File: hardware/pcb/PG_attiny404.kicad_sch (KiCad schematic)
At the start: 30 parts, among them J1 0022232041, J2 Conn_01x01_Male, J3 Conn_01x01_Male, J4 Conn_01x01_Male, J5 Conn_01x01_Male, J6 Conn_01x01_Male, J7 Conn_01x01_Male, J8 Conn_01x01_Male, J9 Conn_01x01_Male, Q1 2N7002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

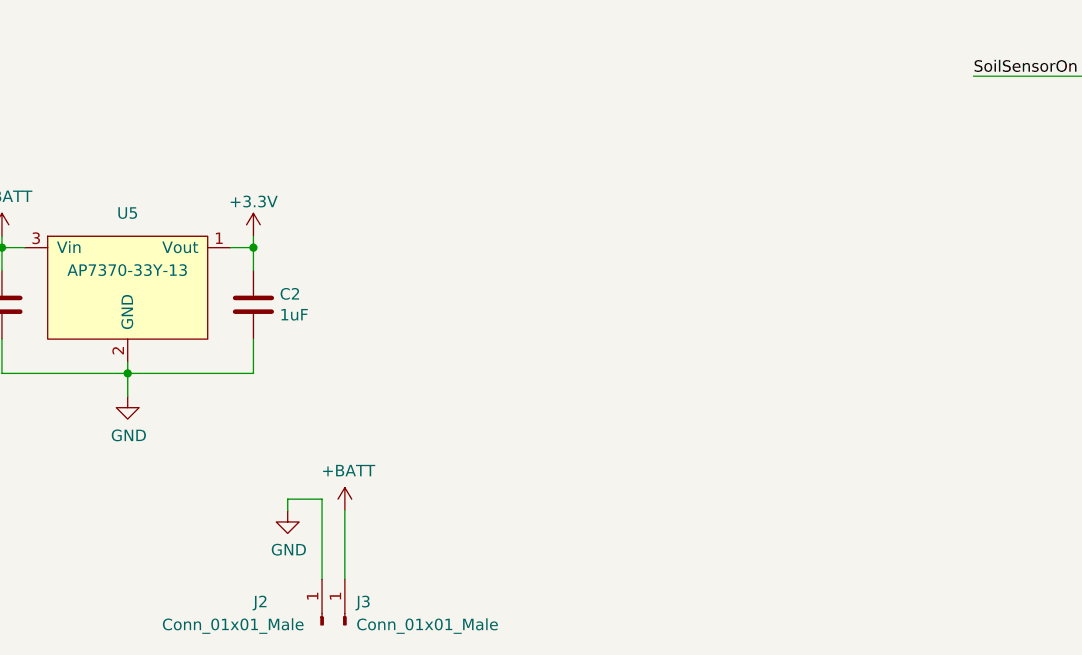
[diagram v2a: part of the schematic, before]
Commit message: Added Reverse voltage protection on PCB
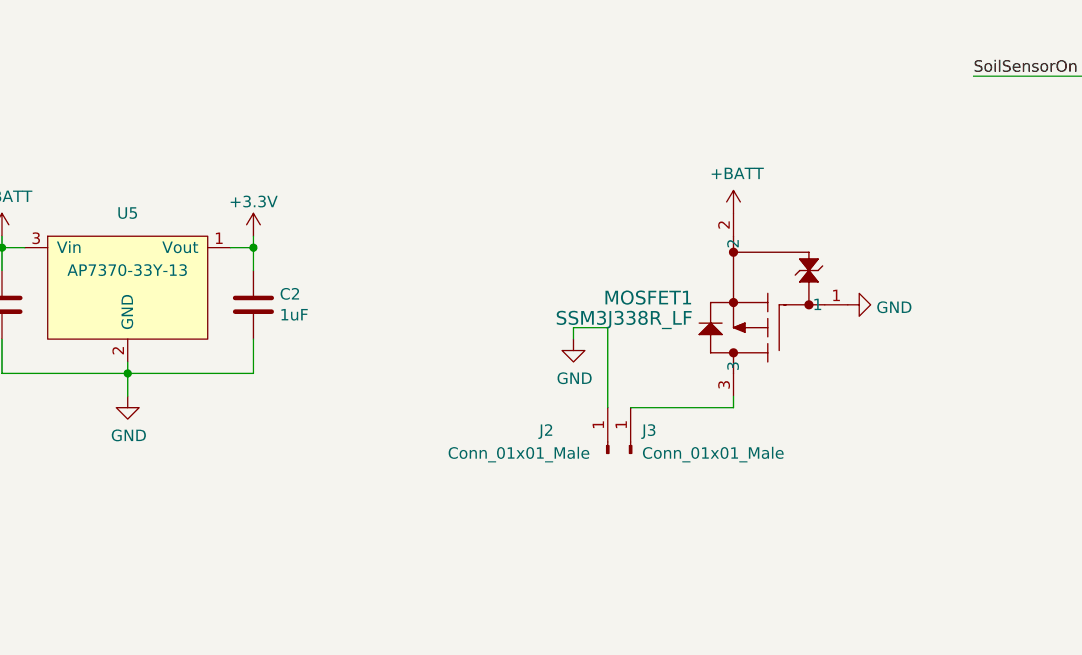
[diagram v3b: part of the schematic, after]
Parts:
- added MOSFET1: SSM3J338R_LF, SOT23:SOT-23F_TOS-L, symbol SSM3J338R_LF:SSM3J338R_LF
- J1: footprint Connector_PinHeader_2.54mm:PinHeader_1x04_P2.54mm_Horizontal -> SOT23:PinHeader_1x04_P2.54mm_Horizontal_spezial
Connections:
- net +BATT: now also MOSFET1.2; no longer J3.1 (Pin_1)
- net GND: now also MOSFET1.1
- new net: J3.1 (Pin_1), MOSFET1.3
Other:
- moved on the sheet: J2, J3
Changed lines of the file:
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@@
+    (stroke (width 0) (type default))
+  )
+  (wire (pts (xy 96.52 168.91) (xy 107.95 168.91))
     (stroke (width 0) (type default))
   )
@@
     (stroke (width 0) (type default))
   )
+  (wire (pts (xy 107.95 168.91) (xy 107.95 167.64))
+    (stroke (width 0) (type default))
+  )
   (wire (pts (xy 132.08 113.03) (xy 156.21 113.03))
     (stroke (width 0) (type default))
@@
     (stroke (width 0) (type default))
   )
-  (wire (pts (xy 62.23 179.07) (xy 62.23 187.96))
+  (wire (pts (xy 93.98 160.02) (xy 93.98 168.91))
     (stroke (width 0) (type default))
   )
@@
     (stroke (width 0) (type default))
   )
-  (wire (pts (xy 58.42 179.07) (xy 58.42 180.34))
+  (wire (pts (xy 90.17 160.02) (xy 90.17 161.29))
     (stroke (width 0) (type default))
   )
@@
     (stroke (width 0) (type default))
   )
-  (wire (pts (xy 62.23 179.07) (xy 58.42 179.07))
+  (wire (pts (xy 93.98 160.02) (xy 90.17 160.02))
     (stroke (width 0) (type default))
   )
@@
   )
   (wire (pts (xy 26.67 161.29) (xy 26.67 165.1))
-    (stroke (width 0) (type default))
-  )
-  (wire (pts (xy 64.77 180.34) (xy 64.77 187.96))
     (stroke (width 0) (type default))
   )
@@
       (effects (font (size 1.27 1.27)) (justify right))
     )
-    (property "Footprint" "Connector_PinHeader_2.54mm:PinHeader_1x04_P2.54mm_Horizontal" (at 109.22 49.53 0)
+    (property "Footprint" "SOT23:PinHeader_1x04_P2.54mm_Horizontal_spezial" (at 109.22 49.53 0)
       (effects (font (size 1.524 1.524)) (justify left) hide)
     )
@@
     )
   )
-  (symbol (lib_id "Connector:Conn_01x01_Male") (at 62.23 193.04 90) (unit 1)
-    (in_bom yes) (on_board yes) (dnp no)
-    (property "Reference" "J2" (at 54.61 190.5 90)
-      (effects (font (size 1.27 1.27)) (justify right))
-    )
-    (property "Value" "Conn_01x01_Male" (at 44.45 193.04 90)
-      (effects (font (size 1.27 1.27)) (justify right))
-    )
-    (property "Footprint" "digikey-footprints:PROBE_PAD_1206" (at 62.23 193.04 0)
-      (effects (font (size 1.27 1.27)) hide)
-    )
-    (property "Datasheet" "~" (at 62.23 193.04 0)
+  (symbol (lib_id "Connector:Conn_01x01_Male") (at 93.98 173.99 90) (unit 1)
+    (in_bom yes) (on_board yes) (dnp no)
+    (property "Reference" "J2" (at 86.36 171.45 90)
+      (effects (font (size 1.27 1.27)) (justify right))
+    )
+    (property "Value" "Conn_01x01_Male" (at 76.2 173.99 90)
+      (effects (font (size 1.27 1.27)) (justify right))
+    )
+    (property "Footprint" "digikey-footprints:PROBE_PAD_1206" (at 93.98 173.99 0)
+      (effects (font (size 1.27 1.27)) hide)
+    )
+    (property "Datasheet" "~" (at 93.98 173.99 0)
       (effects (font (size 1.27 1.27)) hide)
     )
@@
     )
   )
-  (symbol (lib_id "Connector:Conn_01x01_Male") (at 64.77 193.04 90) (unit 1)
-    (in_bom yes) (on_board yes) (dnp no)
-    (property "Reference" "J3" (at 66.04 190.5 90)
-      (effects (font (size 1.27 1.27)) (justify right))
-    )
-    (property "Value" "Conn_01x01_Male" (at 66.04 193.04 90)
-      (effects (font (size 1.27 1.27)) (justify right))
-    )
-    (property "Footprint" "digikey-footprints:PROBE_PAD_1206" (at 64.77 193.04 0)
-      (effects (font (size 1.27 1.27)) hide)
-    )
-    (property "Datasheet" "~" (at 64.77 193.04 0)
+  (symbol (lib_id "Connector:Conn_01x01_Male") (at 96.52 173.99 90) (unit 1)
+    (in_bom yes) (on_board yes) (dnp no)
+    (property "Reference" "J3" (at 97.79 171.45 90)
+      (effects (font (size 1.27 1.27)) (justify right))
+    )
+    (property "Value" "Conn_01x01_Male" (at 97.79 173.99 90)
+      (effects (font (size 1.27 1.27)) (justify right))
+    )
+    (property "Footprint" "digikey-footprints:PROBE_PAD_1206" (at 96.52 173.99 0)
+      (effects (font (size 1.27 1.27)) hide)
+    )
+    (property "Datasheet" "~" (at 96.52 173.99 0)
       (effects (font (size 1.27 1.27)) hide)
     )
@@
     )
   )
-  (symbol (lib_id "power:+BATT") (at 64.77 180.34 0) (unit 1)
-    (in_bom yes) (on_board yes) (dnp no)
-    (property "Reference" "#PWR016" (at 64.77 184.15 0)
-      (effects (font (size 1.27 1.27)) hide)
-    )
-    (property "Value" "+BATT" (at 65.151 175.9458 0)
-      (effects (font (size 1.27 1.27)))
-    )
-    (property "Footprint" "" (at 64.77 180.34 0)
-      (effects (font (size 1.27 1.27)) hide)
-    )
-    (property "Datasheet" "" (at 64.77 180.34 0)
+  (symbol (lib_id "power:+BATT") (at 107.95 147.32 0) (unit 1)
+    (in_bom yes) (on_board yes) (dnp no)
+    (property "Reference" "#PWR016" (at 107.95 151.13 0)
+      (effects (font (size 1.27 1.27)) hide)
+    )
+    (property "Value" "+BATT" (at 108.331 142.9258 0)
+      (effects (font (size 1.27 1.27)))
+    )
+    (property "Footprint" "" (at 107.95 147.32 0)
+      (effects (font (size 1.27 1.27)) hide)
+    )
+    (property "Datasheet" "" (at 107.95 147.32 0)
       (effects (font (size 1.27 1.27)) hide)
     )
@@
     )
   )
-  (symbol (lib_id "power:GND") (at 58.42 180.34 0) (unit 1)
-    (in_bom yes) (on_board yes) (dnp no)
-    (property "Reference" "#PWR015" (at 58.42 186.69 0)
-      (effects (font (size 1.27 1.27)) hide)
-    )
-    (property "Value" "GND" (at 58.547 184.7342 0)
-      (effects (font (size 1.27 1.27)))
-    )
-    (property "Footprint" "" (at 58.42 180.34 0)
-      (effects (font (size 1.27 1.27)) hide)
-    )
-    (property "Datasheet" "" (at 58.42 180.34 0)
+  (symbol (lib_id "power:GND") (at 90.17 161.29 0) (unit 1)
+    (in_bom yes) (on_board yes) (dnp no)
+    (property "Reference" "#PWR015" (at 90.17 167.64 0)
+      (effects (font (size 1.27 1.27)) hide)
+    )
+    (property "Value" "GND" (at 90.297 165.6842 0)
+      (effects (font (size 1.27 1.27)))
+    )
+    (property "Footprint" "" (at 90.17 161.29 0)
+      (effects (font (size 1.27 1.27)) hide)
+    )
+    (property "Datasheet" "" (at 90.17 161.29 0)
       (effects (font (size 1.27 1.27)) hide)
     )
@@
         (path "/e68a78e5-8846-4666-9105-5fa8784d19c8"
           (reference "D1") (unit 1)
+        )
+      )
+    )
+  )
+  (symbol (lib_name "GND_1") (lib_id "power:GND") (at 120.65 157.48 90) (unit 1)
+    (in_bom yes) (on_board yes) (dnp no) (fields_autoplaced)
+    (property "Reference" "#PWR020" (at 127 157.48 0)
+      (effects (font (size 1.27 1.27)) hide)
+    )
+    (property "Value" "GND" (at 123.825 157.7968 90)
+      (effects (font (size 1.27 1.27)) (justify right))
+    )
+    (property "Footprint" "" (at 120.65 157.48 0)
+      (effects (font (size 1.27 1.27)) hide)
+    )
+    (property "Datasheet" "" (at 120.65 157.48 0)
+      (effects (font (size 1.27 1.27)) hide)
+    )
+    (pin "1")
+    (instances
+      (project "PG_attiny404"
+        (path "/e68a78e5-8846-4666-9105-5fa8784d19c8"
+          (reference "#PWR020") (unit 1)
         )
       )
@@
         )
       )
+    )
+  )
+  (symbol (lib_id "SSM3J338R_LF:SSM3J338R_LF") (at 118.11 165.1 180) (unit 1)
+    (in_bom yes) (on_board yes) (dnp no) (fields_autoplaced)
+    (property "Reference" "MOSFET1" (at 103.4289 156.733 0)
+      (effects (font (size 1.524 1.524)) (justify left))
+    )
+    (property "Value" "SSM3J338R_LF" (at 103.4289 158.9872 0)
+      (effects (font (size 1.524 1.524)) (justify left))
+    )
+    (property "Footprint" "SOT23:SOT-23F_TOS-L" (at 118.11 165.1 0)
+      (effects (font (size 1.27 1.27) italic) hide)
+    )
+    (property "Datasheet" "SSM3J338R_LF" (at 118.11 165.1 0)
+      (effects (font (size 1.27 1.27) italic) hide)
+    )
+    (property "DK_Detail_Page" "https://www.digikey.at/de/products/detail/toshiba-semiconductor-and-storage/SSM3J338R-LF/5810226" (at 118.11 165.1 0)
+      (effects (font (size 1.27 1.27)) hide)
+    )
+    (pin "1")
+    (pin "2")
+    (pin "3")
+    (instances
+      (project "PG_attiny404"
+        (path "/e68a78e5-8846-4666-9105-5fa8784d19c8"
+          (reference "MOSFET1") (unit 1)
+        )
+      )

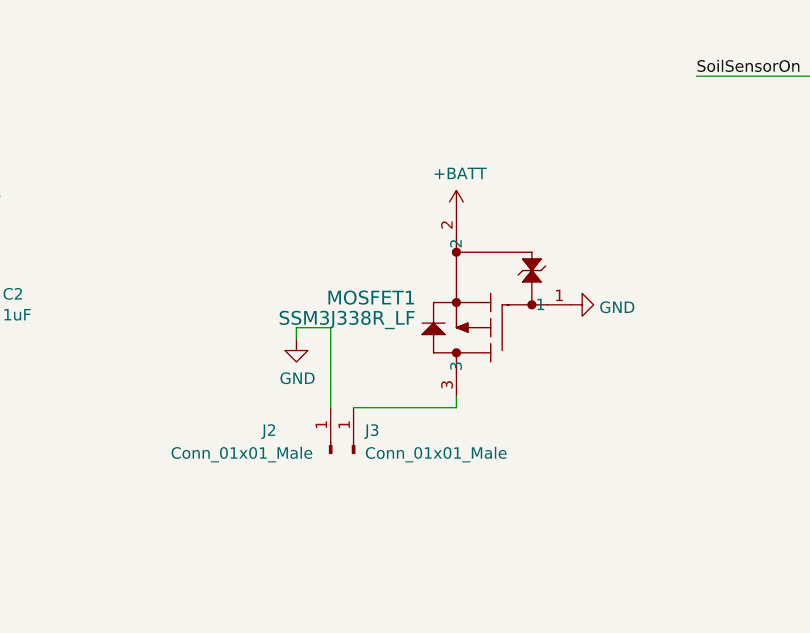
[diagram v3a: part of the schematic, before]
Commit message: Motor code polishing, Added p-channel to pcb for reverse voltage protection
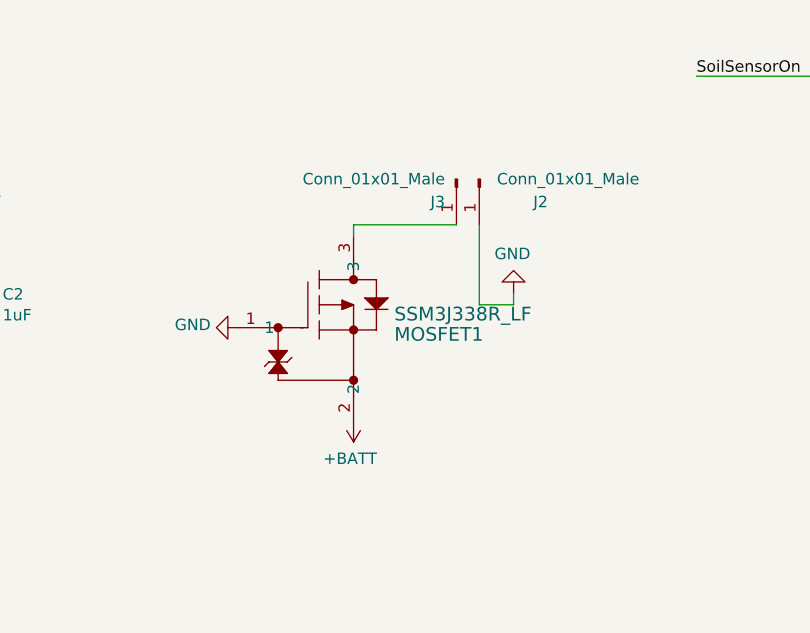
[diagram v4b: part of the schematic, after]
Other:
- moved on the sheet: J2, J3, MOSFET1
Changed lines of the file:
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@@
     (stroke (width 0) (type default))
   )
-  (wire (pts (xy 96.52 168.91) (xy 107.95 168.91))
+  (wire (pts (xy 107.95 148.59) (xy 96.52 148.59))
     (stroke (width 0) (type default))
   )
@@
     (stroke (width 0) (type default))
   )
-  (wire (pts (xy 107.95 168.91) (xy 107.95 167.64))
+  (wire (pts (xy 96.52 148.59) (xy 96.52 149.86))
     (stroke (width 0) (type default))
   )
@@
     (stroke (width 0) (type default))
   )
-  (wire (pts (xy 93.98 160.02) (xy 93.98 168.91))
+  (wire (pts (xy 110.49 157.48) (xy 110.49 148.59))
     (stroke (width 0) (type default))
   )
@@
     (stroke (width 0) (type default))
   )
-  (wire (pts (xy 90.17 160.02) (xy 90.17 161.29))
+  (wire (pts (xy 114.3 157.48) (xy 114.3 156.21))
     (stroke (width 0) (type default))
   )
@@
     (stroke (width 0) (type default))
   )
-  (wire (pts (xy 93.98 160.02) (xy 90.17 160.02))
+  (wire (pts (xy 110.49 157.48) (xy 114.3 157.48))
     (stroke (width 0) (type default))
   )
@@
     )
   )
-  (symbol (lib_id "Connector:Conn_01x01_Male") (at 93.98 173.99 90) (unit 1)
-    (in_bom yes) (on_board yes) (dnp no)
-    (property "Reference" "J2" (at 86.36 171.45 90)
-      (effects (font (size 1.27 1.27)) (justify right))
-    )
-    (property "Value" "Conn_01x01_Male" (at 76.2 173.99 90)
-      (effects (font (size 1.27 1.27)) (justify right))
-    )
-    (property "Footprint" "digikey-footprints:PROBE_PAD_1206" (at 93.98 173.99 0)
-      (effects (font (size 1.27 1.27)) hide)
-    )
-    (property "Datasheet" "~" (at 93.98 173.99 0)
+  (symbol (lib_id "Connector:Conn_01x01_Male") (at 110.49 143.51 270) (unit 1)
+    (in_bom yes) (on_board yes) (dnp no)
+    (property "Reference" "J2" (at 118.11 146.05 90)
+      (effects (font (size 1.27 1.27)) (justify right))
+    )
+    (property "Value" "Conn_01x01_Male" (at 128.27 143.51 90)
+      (effects (font (size 1.27 1.27)) (justify right))
+    )
+    (property "Footprint" "digikey-footprints:PROBE_PAD_1206" (at 110.49 143.51 0)
+      (effects (font (size 1.27 1.27)) hide)
+    )
+    (property "Datasheet" "~" (at 110.49 143.51 0)
       (effects (font (size 1.27 1.27)) hide)
     )
@@
     )
   )
-  (symbol (lib_id "Connector:Conn_01x01_Male") (at 96.52 173.99 90) (unit 1)
-    (in_bom yes) (on_board yes) (dnp no)
-    (property "Reference" "J3" (at 97.79 171.45 90)
-      (effects (font (size 1.27 1.27)) (justify right))
-    )
-    (property "Value" "Conn_01x01_Male" (at 97.79 173.99 90)
-      (effects (font (size 1.27 1.27)) (justify right))
-    )
-    (property "Footprint" "digikey-footprints:PROBE_PAD_1206" (at 96.52 173.99 0)
-      (effects (font (size 1.27 1.27)) hide)
-    )
-    (property "Datasheet" "~" (at 96.52 173.99 0)
+  (symbol (lib_id "Connector:Conn_01x01_Male") (at 107.95 143.51 270) (unit 1)
+    (in_bom yes) (on_board yes) (dnp no)
+    (property "Reference" "J3" (at 106.68 146.05 90)
+      (effects (font (size 1.27 1.27)) (justify right))
+    )
+    (property "Value" "Conn_01x01_Male" (at 106.68 143.51 90)
+      (effects (font (size 1.27 1.27)) (justify right))
+    )
+    (property "Footprint" "digikey-footprints:PROBE_PAD_1206" (at 107.95 143.51 0)
+      (effects (font (size 1.27 1.27)) hide)
+    )
+    (property "Datasheet" "~" (at 107.95 143.51 0)
       (effects (font (size 1.27 1.27)) hide)
     )
@@
     )
   )
-  (symbol (lib_id "power:+BATT") (at 107.95 147.32 0) (unit 1)
-    (in_bom yes) (on_board yes) (dnp no)
-    (property "Reference" "#PWR016" (at 107.95 151.13 0)
-      (effects (font (size 1.27 1.27)) hide)
-    )
-    (property "Value" "+BATT" (at 108.331 142.9258 0)
-      (effects (font (size 1.27 1.27)))
-    )
-    (property "Footprint" "" (at 107.95 147.32 0)
-      (effects (font (size 1.27 1.27)) hide)
-    )
-    (property "Datasheet" "" (at 107.95 147.32 0)
+  (symbol (lib_id "power:+BATT") (at 96.52 170.18 180) (unit 1)
+    (in_bom yes) (on_board yes) (dnp no)
+    (property "Reference" "#PWR016" (at 96.52 166.37 0)
+      (effects (font (size 1.27 1.27)) hide)
+    )
+    (property "Value" "+BATT" (at 96.139 174.5742 0)
+      (effects (font (size 1.27 1.27)))
+    )
+    (property "Footprint" "" (at 96.52 170.18 0)
+      (effects (font (size 1.27 1.27)) hide)
+    )
+    (property "Datasheet" "" (at 96.52 170.18 0)
       (effects (font (size 1.27 1.27)) hide)
     )
@@
     )
   )
-  (symbol (lib_id "power:GND") (at 90.17 161.29 0) (unit 1)
-    (in_bom yes) (on_board yes) (dnp no)
-    (property "Reference" "#PWR015" (at 90.17 167.64 0)
-      (effects (font (size 1.27 1.27)) hide)
-    )
-    (property "Value" "GND" (at 90.297 165.6842 0)
-      (effects (font (size 1.27 1.27)))
-    )
-    (property "Footprint" "" (at 90.17 161.29 0)
-      (effects (font (size 1.27 1.27)) hide)
-    )
-    (property "Datasheet" "" (at 90.17 161.29 0)
+  (symbol (lib_id "power:GND") (at 114.3 156.21 180) (unit 1)
+    (in_bom yes) (on_board yes) (dnp no)
+    (property "Reference" "#PWR015" (at 114.3 149.86 0)
+      (effects (font (size 1.27 1.27)) hide)
+    )
+    (property "Value" "GND" (at 114.173 151.8158 0)
+      (effects (font (size 1.27 1.27)))
+    )
+    (property "Footprint" "" (at 114.3 156.21 0)
+      (effects (font (size 1.27 1.27)) hide)
+    )
+    (property "Datasheet" "" (at 114.3 156.21 0)
       (effects (font (size 1.27 1.27)) hide)
     )
@@
     )
   )
-  (symbol (lib_name "GND_1") (lib_id "power:GND") (at 120.65 157.48 90) (unit 1)
+  (symbol (lib_name "GND_1") (lib_id "power:GND") (at 83.82 160.02 270) (unit 1)
     (in_bom yes) (on_board yes) (dnp no) (fields_autoplaced)
-    (property "Reference" "#PWR020" (at 127 157.48 0)
-      (effects (font (size 1.27 1.27)) hide)
-    )
-    (property "Value" "GND" (at 123.825 157.7968 90)
-      (effects (font (size 1.27 1.27)) (justify right))
-    )
-    (property "Footprint" "" (at 120.65 157.48 0)
-      (effects (font (size 1.27 1.27)) hide)
-    )
-    (property "Datasheet" "" (at 120.65 157.48 0)
+    (property "Reference" "#PWR020" (at 77.47 160.02 0)
+      (effects (font (size 1.27 1.27)) hide)
+    )
+    (property "Value" "GND" (at 80.645 159.7032 90)
+      (effects (font (size 1.27 1.27)) (justify right))
+    )
+    (property "Footprint" "" (at 83.82 160.02 0)
+      (effects (font (size 1.27 1.27)) hide)
+    )
+    (property "Datasheet" "" (at 83.82 160.02 0)
       (effects (font (size 1.27 1.27)) hide)
     )
@@
     )
   )
-  (symbol (lib_id "SSM3J338R_LF:SSM3J338R_LF") (at 118.11 165.1 180) (unit 1)
+  (symbol (lib_id "SSM3J338R_LF:SSM3J338R_LF") (at 86.36 152.4 0) (unit 1)
     (in_bom yes) (on_board yes) (dnp no) (fields_autoplaced)
-    (property "Reference" "MOSFET1" (at 103.4289 156.733 0)
+    (property "Reference" "MOSFET1" (at 101.0411 160.767 0)
       (effects (font (size 1.524 1.524)) (justify left))
     )
-    (property "Value" "SSM3J338R_LF" (at 103.4289 158.9872 0)
+    (property "Value" "SSM3J338R_LF" (at 101.0411 158.5128 0)
       (effects (font (size 1.524 1.524)) (justify left))
     )
-    (property "Footprint" "SOT23:SOT-23F_TOS-L" (at 118.11 165.1 0)
+    (property "Footprint" "SOT23:SOT-23F_TOS-L" (at 86.36 152.4 0)
       (effects (font (size 1.27 1.27) italic) hide)
     )
-    (property "Datasheet" "SSM3J338R_LF" (at 118.11 165.1 0)
+    (property "Datasheet" "SSM3J338R_LF" (at 86.36 152.4 0)
       (effects (font (size 1.27 1.27) italic) hide)
     )
-    (property "DK_Detail_Page" "https://www.digikey.at/de/products/detail/toshiba-semiconductor-and-storage/SSM3J338R-LF/5810226" (at 118.11 165.1 0)
-      (effects (font (size 1.27 1.27)) hide)
-    )
+    (property "DK_Detail_Page" "https://www.digikey.at/de/products/detail/toshiba-semiconductor-and-storage/SSM3J338R-LF/5810226" (at 86.36 152.4 0)
+      (effects (font (size 1.27 1.27)) hide)
+    )
